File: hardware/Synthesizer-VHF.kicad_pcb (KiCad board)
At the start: 4 copper layers, 50.6 x 50.6 mm, 110 parts, among them J10 REF_OUT, J12 UPDI, J2 Scope, J4 USB-C 2.0 16P, J5 REF_IN, J7 RFOUTA, J9 RFOUTB, U11 SN74LVC1GU04DBVR, U12 ADF4002BCPZ, U13 SN74LVC1GU04DBVR, U2 FT231XQ, U3 ATtiny1616-M, U4 ADF4351, U5 USBLC6-2SC6, U6 LP5907MFX-3.3, U8 LP5907MFX-3.3, X1 IQXT-220-2 10MHz

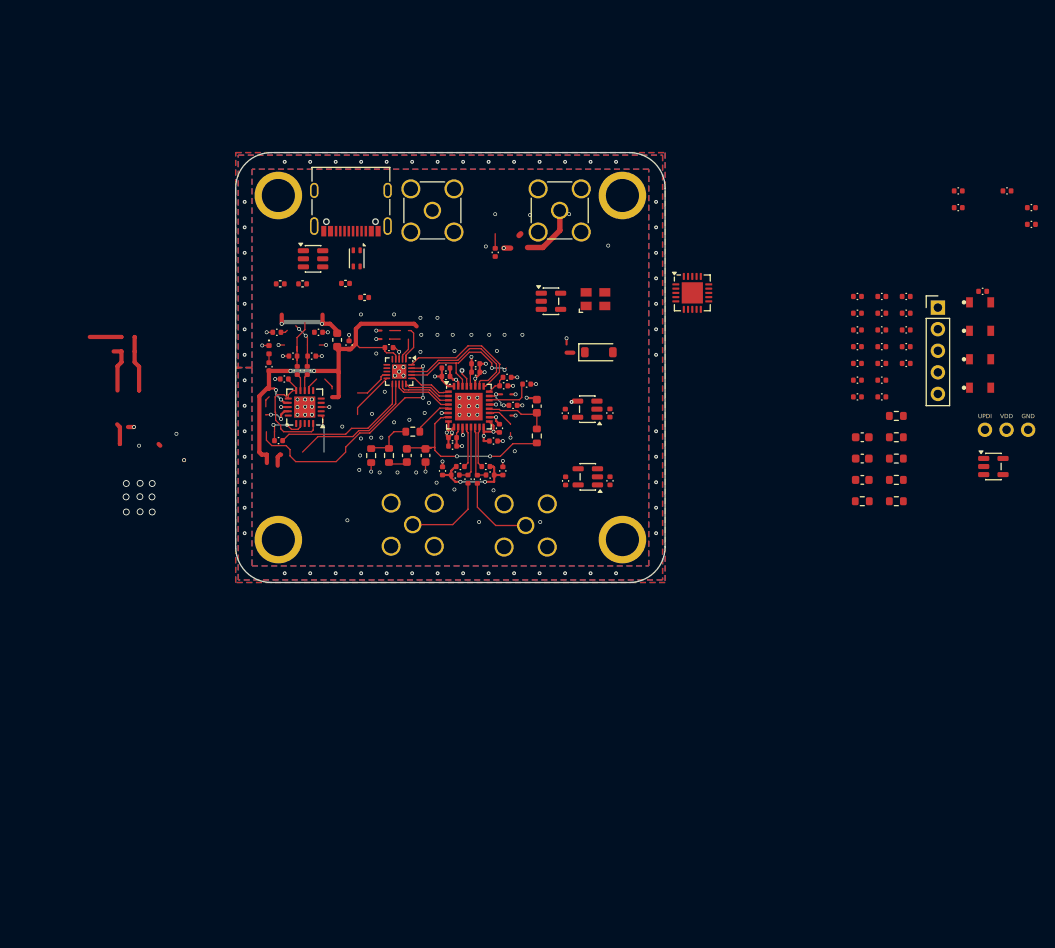
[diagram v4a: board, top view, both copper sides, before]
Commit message: cleanup prior to simplifying the design
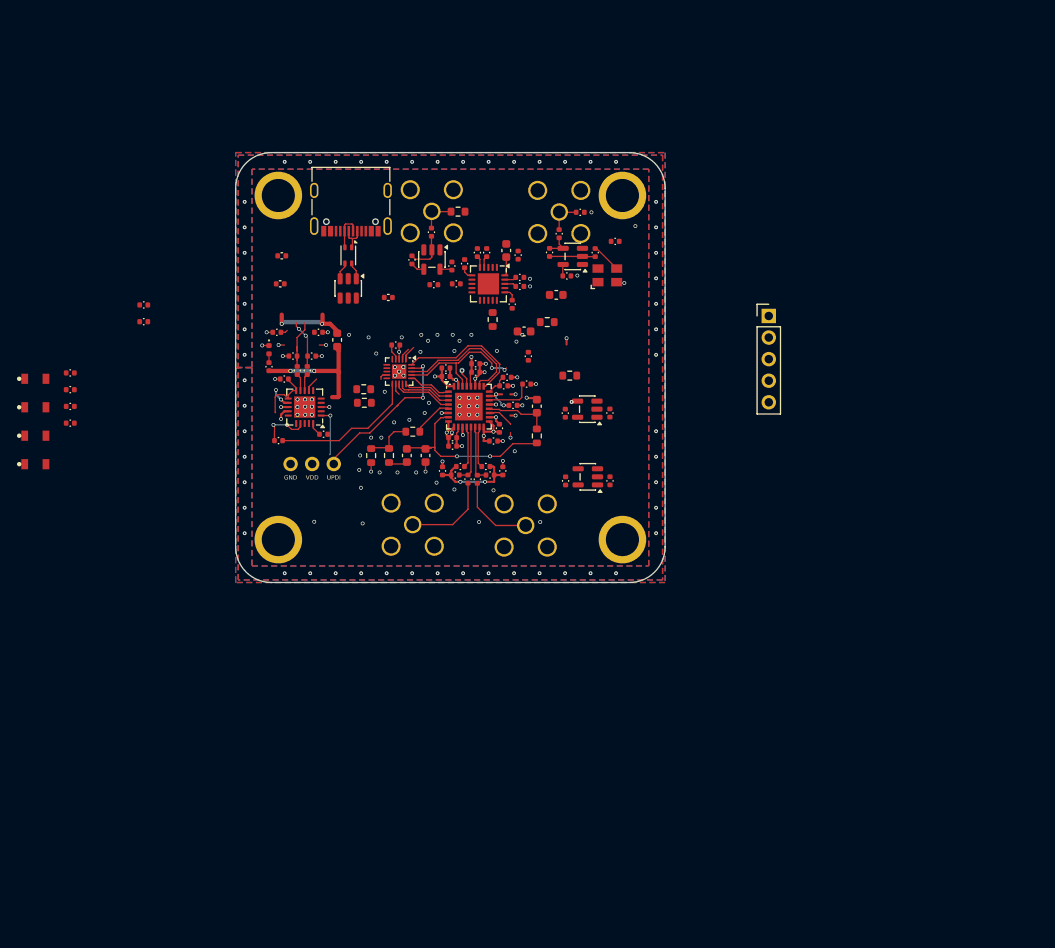
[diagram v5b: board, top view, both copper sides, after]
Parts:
- removed C2: 100n, Synthesizer:Cap_0402
- removed C40: 1u, Capacitor_SMD:C_0402_1005Metric
- removed D9: B5819W, Diode_SMD:D_SOD-123
- J10, J5: moved to B.Cu
- moved D11 111.6 mm to (105.2, 96.2)
- moved D12 111.6 mm to (105.2, 99.5)
- moved D13 111.6 mm to (105.2, 102.9)
- moved D14 111.6 mm to (105.2, 106.2)
- moved R37 98.8 mm to (109.3, 95.5)
- moved R38 98.8 mm to (109.3, 97.5)
- moved R39 98.8 mm to (109.3, 99.4)
- moved R40 98.8 mm to (109.3, 101.4)
- moved R33 87.0 mm to (117.9, 89.5)
- moved C54 84.0 mm to (117.9, 87.5)
- moved J12 81.8 mm to (137.8, 106.2), turned to 180 degrees
- moved U13 70.4 mm to (151.8, 82.1), turned to -90 degrees
- moved C63 67.2 mm to (139.1, 102.7)
- moved R48 63.6 mm to (143.8, 97.4), turned to 180 degrees
- moved R47 63.0 mm to (143.9, 99.0), turned to 180 degrees
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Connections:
- net /COMM_K renamed Net-(D14-K)
- net /PWR_A renamed Net-(D11-A)
- net /REFLED renamed Net-(D12-A)
- net /REF_IN renamed Net-(C58-Pad1)
- net /SYNLED renamed Net-(D13-A)
- C42 pad 1: /5V_USB -> /5V
- C43 pad 1: /5V_USB -> /5V
- FB1 pad 2: /5V_USB -> /5V
- R28 pad 2: /BUF -> Net-(R28-Pad2)
- R29 pad 2: /BUF -> Net-(R28-Pad2)
- U11 pad 4: /BUF -> Net-(R28-Pad2)
- U3 pad 1: unconnected-(U3-PA2-Pad1) -> /DBG1
- U3 pad 2: unconnected-(U3-PA3-Pad2) -> /DBG2
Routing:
- net /5V: track 48.7 -> 17.1 mm
- net (no net): track 18.6 -> 0.00 mm
- net /TXD_M: track 20.1 -> 7.12 mm
- net GND: track 45.6 -> 34.7 mm, vias 169 -> 151
- net /UPDI: track 29.5 -> 19.2 mm
- net /VDD: track 7.52 -> 15.4 mm
- net /3V3: track 14.0 -> 7.09 mm
- net /REF_LOCK: track 5.68 -> 0.00 mm
- net Net-(C50-Pad2): track 0.00 -> 5.38 mm
- net Net-(C4-Pad1): track 0.00 -> 5.09 mm
- net Net-(J4-D+-PadA6): track 0.00 -> 4.50 mm
- net unconnected-(U3-PA2-Pad1): track 4.19 -> 0.00 mm
- net /REF_OUT: track 0.00 -> 4.09 mm
- net Net-(J4-D--PadA7): track 0.00 -> 3.67 mm
- net /XO: track 0.00 -> 3.54 mm
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
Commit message: diecast-2x2: external 10 MHz with TCXO fallback, drop ADF4002
Remove the ADF4002 disciplining loop, the VCTCXO, and REF OUT.
Keep the REF IN squarer. Add a 10 MHz TCXO, a Schmitt buffer, and a
74LVC1G157 so PA6 selects the reference and PA5 watches REF IN.
New parts are parked off the board. Existing placement is unchanged.

Co-authored-by: Jeffrey Millar <wa1hco@users.noreply.github.com>
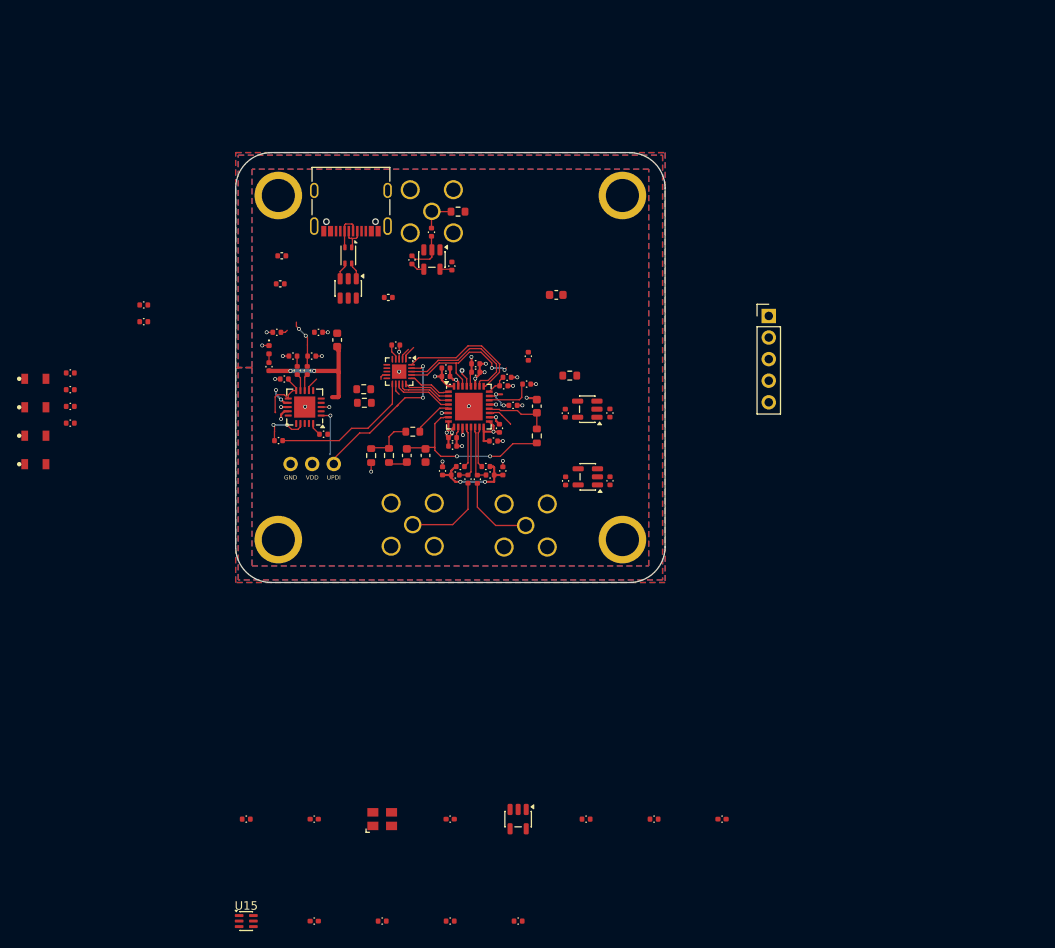
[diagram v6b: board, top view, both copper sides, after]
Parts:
- removed C34, C59: 100p, Synthesizer:Cap_0402
- removed C5, C50, C51, C57, C58, C60, C61, C65: 100n, Synthesizer:Cap_0402
- removed C55: 150p, Capacitor_SMD:C_0603_1608Metric
- removed C56: 2.2n, Capacitor_SMD:C_0603_1608Metric
- removed J10: REF_OUT, Connector_Coaxial:SMA_Amphenol_901-144_Vertical
- removed R28: 1M, Synthesizer:Res_0402
- removed R29: 39R, Synthesizer:Res_0402
- removed R34: 10M, Resistor_SMD:R_0603_1608Metric
- removed R35: 5K1, Synthesizer:Res_0402
- removed R36: 100k, Synthesizer:Res_0402
- removed R44: 33R, Synthesizer:Res_0402
- removed R46: 10k, Resistor_SMD:R_0603_1608Metric
- removed U11: SN74LVC1GU04DBVR, Package_TO_SOT_SMD:SOT-23-5
- removed U12: ADF4002BCPZ, Package_DFN_QFN:QFN-20-1EP_4x4mm_P0.5mm_EP2.5x2.5mm
- removed X1: IQXT-220-2 10MHz, Synthesizer:Oscillator_SMD_3225_VCTCXO
- added C66: 100n, Synthesizer:Cap_0402, F.Cu at (138.0, 148.0)
- added C67: 10n, Synthesizer:Cap_0402, F.Cu at (154.0, 148.0)
- added C68: 100n, Synthesizer:Cap_0402, F.Cu at (186.0, 148.0)
- added C69: 100n, Synthesizer:Cap_0402, F.Cu at (138.0, 160.0)
- added R50: 10R, Synthesizer:Res_0402, F.Cu at (130.0, 148.0)
- added R51: 100k, Synthesizer:Res_0402, F.Cu at (170.0, 148.0)
- added R52: 100k, Synthesizer:Res_0402, F.Cu at (178.0, 148.0)
- added R53: 10k, Synthesizer:Res_0402, F.Cu at (146.0, 160.0)
- added R54: 33R, Synthesizer:Res_0402, F.Cu at (154.0, 160.0)
- added R55: 1k, Synthesizer:Res_0402, F.Cu at (162.0, 160.0)
- added U14: SN74LVC1G17DBVR, Package_TO_SOT_SMD:SOT-23-5, F.Cu at (162.0, 148.0)
- added U15: 74LVC1G157GW, Package_TO_SOT_SMD:SOT-363_SC-70-6, F.Cu at (130.0, 160.0)
- added X2: OW2EL89CEIUXK7YLC-10M, Synthesizer:Oscillator_SMD_3225_VCTCXO, F.Cu at (146.0, 148.0)
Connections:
- net Net-(R30-Pad2) renamed /REF_BUF
- C3 pad 2: /BUF -> /REF_AC
- U3 pad 6: /MUX4002 -> /REF_DET
- U3 pad 7: /DAC_HOLD -> /REF_SEL
- U3 pad 8: /LE4002 -> (no net)
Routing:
- net /VBUS_C: track 9.22 -> 0.00 mm, vias 2 -> 0
- net Net-(C50-Pad2): track 5.38 -> 0.00 mm
- net /USB_DM: track 6.57 -> 1.23 mm
- net GND: track 34.7 -> 29.7 mm, vias 151 -> 30
- net /REF_OUT: track 4.09 -> 0.00 mm
- net /XO: track 3.54 -> 0.00 mm
- net Net-(R28-Pad2): track 3.11 -> 0.00 mm
- net /VDD: track 15.4 -> 12.4 mm
- net /VRF: track 17.4 -> 14.5 mm
- net /CP: track 2.22 -> 0.00 mm
- net Net-(U12-RSET): track 1.39 -> 0.00 mm
- net /RFINB: track 1.39 -> 0.00 mm
- net /RFINA: track 1.39 -> 0.00 mm
- net Net-(U4-CPout): track 22.5 -> 21.3 mm
- net unconnected-(U6-NC-Pad4): vias 1 -> 0
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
